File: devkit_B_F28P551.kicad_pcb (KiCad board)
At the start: 4 copper layers, 27 x 73.7 mm, 26 parts, among them J1 DEVKIT_C2000_ROW_A, J2 DEVKIT_C2000_ROW_B, J4 RESET, U1 TMS320F28P551SG5PM, U2 MCP1700-3302E/TT, U3 MCP1700-3302E/TT

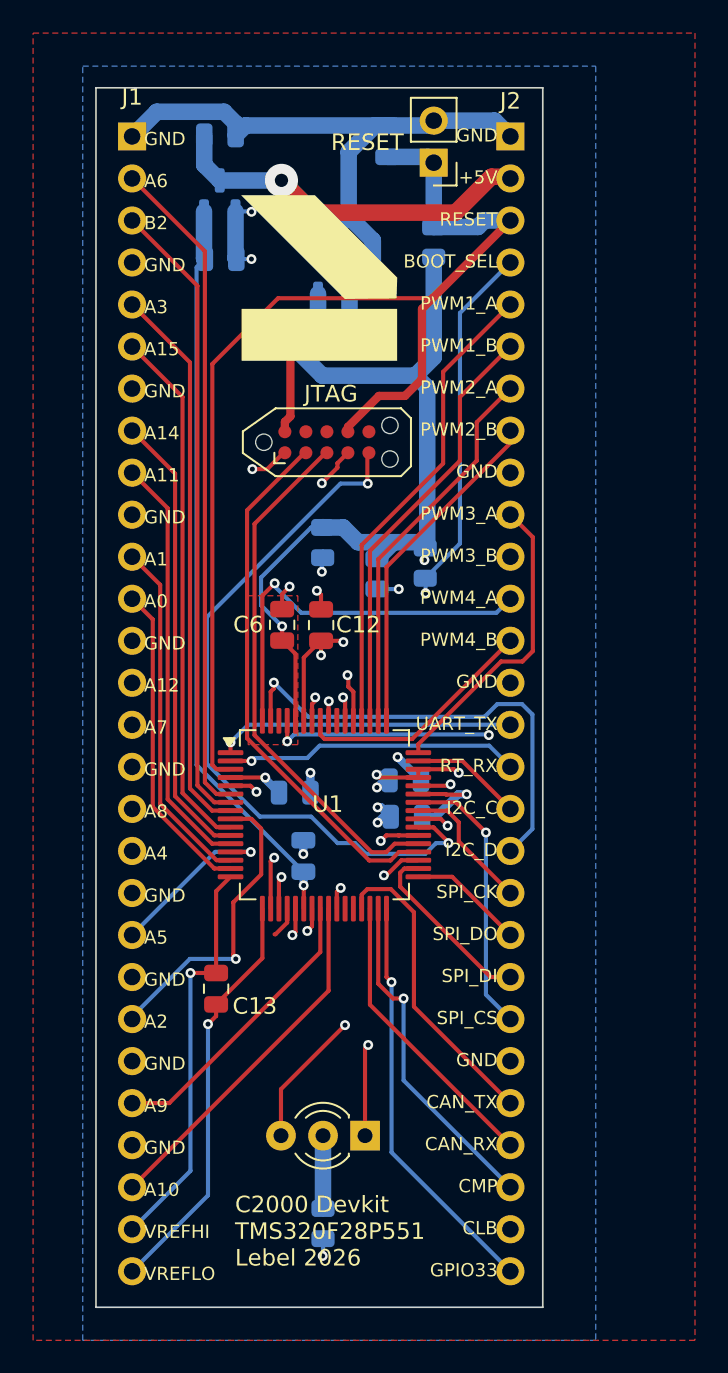
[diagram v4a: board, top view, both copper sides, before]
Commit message: devkit_B_F28P551 : rangee A reroutee pour le CLB (Stage1_EN/Stage2_EN/HV_EN/Discharge), documentation rattrapee
Carte figee, production-ready, modifiee malgre la regle habituelle (decision
explicite de l'utilisateur) : miroir de la decision #20 du depot
KICAD-C2000-powershield cote devkit.

- Rangee A reroutee : Stage1_EN (A23, broche 62/GPIO9), Stage2_EN (A24,
  broche 27/GPIO20), HV_EN (A25, broche 28/GPIO21), Discharge (A26, broche
  55/GPIO41) - six masses pour vingt-deux signaux au lieu de dix pour
  dix-huit.
- Rangee B : nRESET -> ~{RESET} (B3), GPIO_1 -> ~{FAULT_MCU} (B28), logique
  negative, meme net.
- devkit_A_F280037 non modifie (CLB absent du F280037) : le connecteur
  n'est plus identique entre les deux devkits, divergence documentee a la
  decision #13.
- doc/decisions.md : nouvelle decision #13.
- doc/spec-devkit.md, doc/brochage-devkit.csv : rangee A de devkit_B
  consignee comme bloc divergent, devkit_A_F280037 garde la rangee
  d'origine comme reference.

Verification avant commit : kicad-cli pcb drc sur devkit_B_F28P551.kicad_pcb
(0 violation, 0 non connecte) ; kicad-cli sch erc (35 violations, 10
erreurs/25 avertissements, toutes de type deja rencontre ailleurs dans
l'atelier - endpoint_off_grid, pin_not_connected -, aucune nouvelle
categorie).

Co-Authored-By: Claude Sonnet 5 <noreply@anthropic.com>
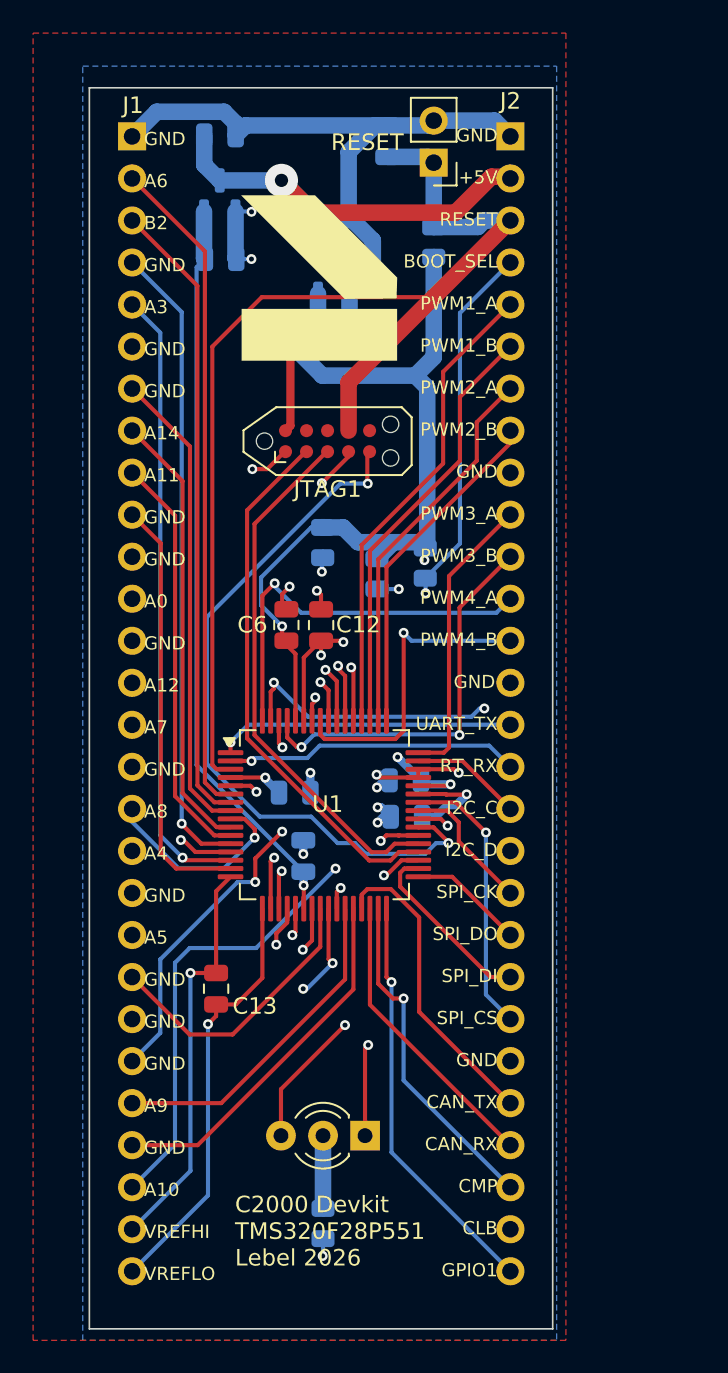
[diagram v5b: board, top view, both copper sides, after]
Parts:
- removed JTAG: Tag-Connect-2050_10, Connector:Tag-Connect_TC2050-IDC-NL_2x05_P1.27mm_Vertical
- added JTAG1: Tag-Connect-2050_10, Connector:Tag-Connect_TC2050-IDC-NL_2x05_P1.27mm_Vertical, F.Cu at (137.8, 65.7)
- moved C6 0.26 mm to (135.3, 76.8)
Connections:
- net GPIO_1 renamed ~{FAULT_MCU}
- net ~{nRESET} renamed ~{RESET}
- J1 pad 10: GND -> ADC_8
- J1 pad 11: Iout -> GND
- J1 pad 12: ADC_8 -> ADC_9
- J1 pad 13: GND -> ADC_10
- J1 pad 14: ADC_9 -> ADC_11
- J1 pad 15: ADC_10 -> ADC_12
- J1 pad 17: ADC_11 -> I_SHUNT1_CMP
- J1 pad 18: ADC_12 -> I_SHUNT1_MES
- J1 pad 20: I_SHUNT1_MES -> I_SHUNT2_CMP
- J1 pad 21: GND -> I_SHUNT2_MES
- J1 pad 22: I_SHUNT1_CMP -> GND
- J1 pad 23: GND -> Stage1_EN
- J1 pad 24: I_SHUNT2_MES -> Stage2_EN
- J1 pad 25: GND -> HV_EN
- J1 pad 26: I_SHUNT2_CMP -> Discharge
- J1 pad 4: GND -> Iin
- J1 pad 5: V1 -> Iout
- J1 pad 6: Temp1 -> GND
- J1 pad 7: GND -> V1
- J1 pad 8: Temp2 -> Temp1
- J1 pad 9: Iin -> Temp2
- U1 pad 27: TP_PIN27 -> Stage2_EN
- U1 pad 28: TP_PIN28 -> HV_EN
- U1 pad 55: TP_PIN55 -> Discharge
- U1 pad 62: TP_PIN62 -> Stage1_EN
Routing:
- net Discharge: track 0.00 -> 42.4 mm, vias 0 -> 2
- net Stage1_EN: track 0.00 -> 25.3 mm, vias 0 -> 3
- net HV_EN: track 0.00 -> 22.2 mm
- net Stage2_EN: track 0.00 -> 20.2 mm
- net Iout: track 21.3 -> 37.7 mm, vias 0 -> 1
- net Iin: track 25.5 -> 38.6 mm, vias 0 -> 1
- net ADC_11: track 13.6 -> 21.9 mm, vias 0 -> 1
- net ADC_12: track 14.9 -> 22.1 mm
- net ADC_8: track 19.3 -> 25.8 mm
- net I_SHUNT1_CMP: track 18.6 -> 12.3 mm
- net ADC_9: track 17.5 -> 23.3 mm
- net V1: track 33.7 -> 28.6 mm
- net Temp1: track 32.0 -> 26.9 mm
- net ADC_10: track 16.0 -> 20.8 mm
- net LED_R: track 30.0 -> 34.3 mm
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- removed copper zone on F.Cu, net VDDIO
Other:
- board size 27 x 73.7 mm -> 28 x 75 mm
- board text added: "GPIO1"
- board text removed: "A1"
- board text removed: "A15"
- board text removed: "A2"
- board text removed: "GPIO33"

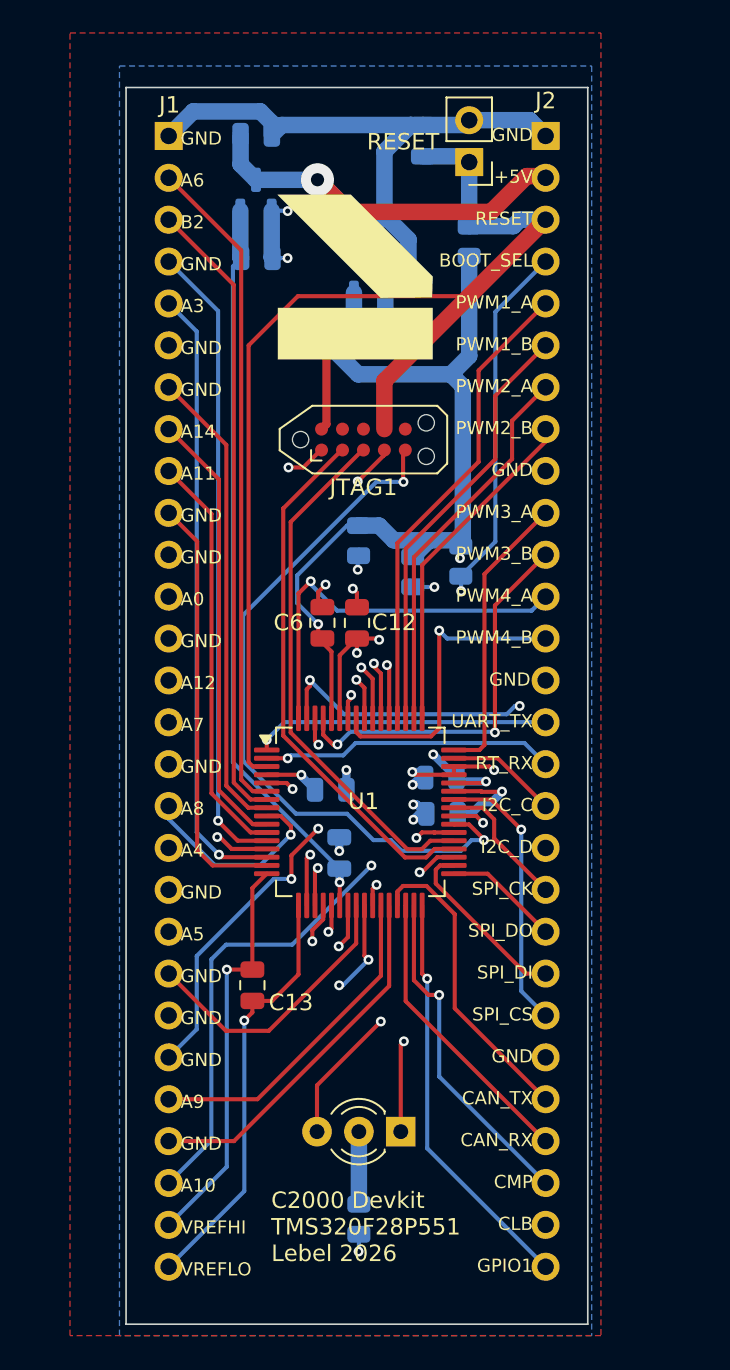
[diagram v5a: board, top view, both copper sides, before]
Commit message: Ajoute le connecteur RKB2SJM250SMTR_LFS et partage TO252
- Connecteur RKB2SJM250SMTR_LFS (lib + modele 3D) integre au connecteur
  devkit, modification de brochage associee (modificatio_brochage_devkit)
  -- travail deja en place localement, jamais commite.
- fp-lib-table : empreinte TO252 partagee enregistree
  (lib_fp_commun/TO252.pretty, voir KICAD.md), pas encore utilisee par
  un composant de ce depot.

Co-Authored-By: Claude Sonnet 5 <noreply@anthropic.com>
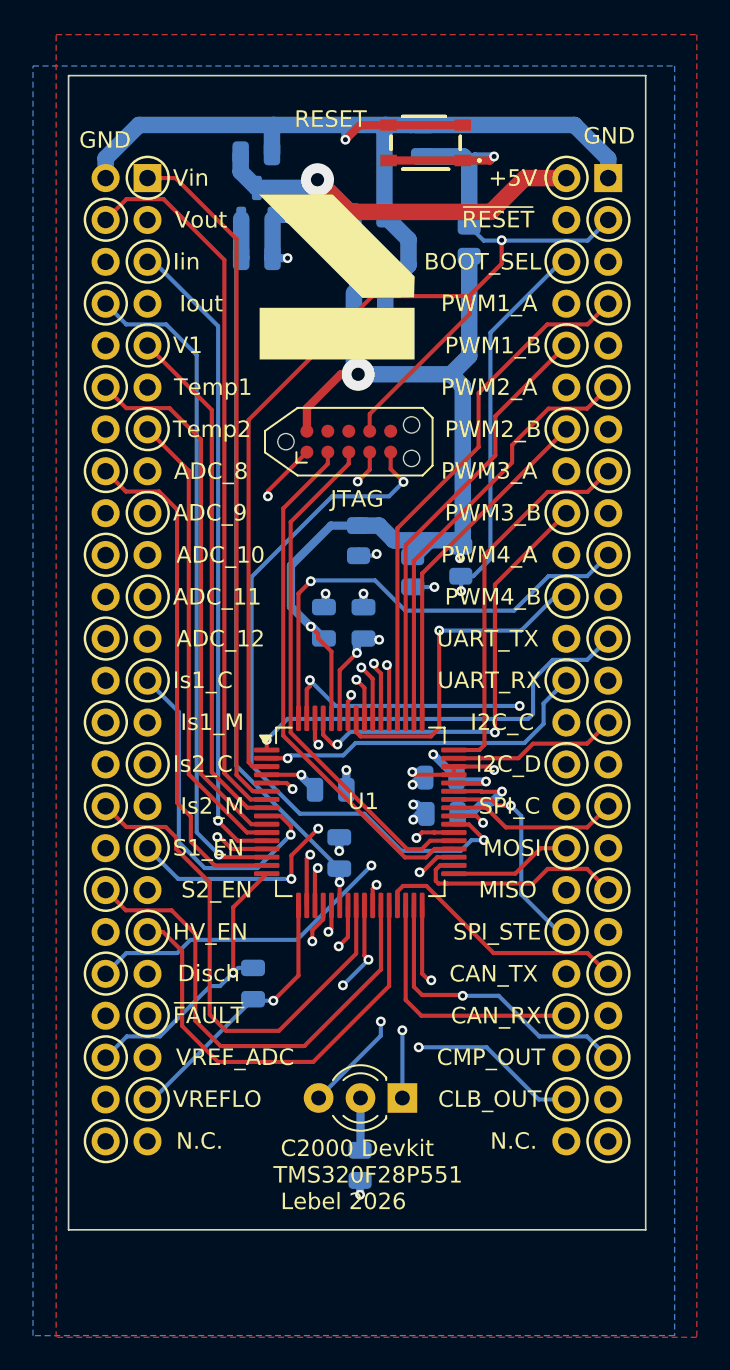
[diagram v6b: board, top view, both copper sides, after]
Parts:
- removed J4: RESET, Connector_PinHeader_2.54mm:PinHeader_1x02_P2.54mm_Vertical
- added S1: RKB2SJM250SMTR_LFS, lib:RKB2SJM250SMTRLFS, F.Cu at (141.6, 47.7)
- C12, C13, C6: moved to B.Cu
- J1: value DEVKIT_C2000_ROW_A -> DEVKIT_C2000_A; footprint Connector_PinHeader_2.54mm:PinHeader_1x28_P2.54mm_Vertical -> Connector_PinHeader_2.54mm:PinHeader_2x24_P2.54mm_Vertical
- J2: value DEVKIT_C2000_ROW_B -> DEVKIT_C2000_B; footprint Connector_PinHeader_2.54mm:PinHeader_1x28_P2.54mm_Vertical -> Connector_PinHeader_2.54mm:PinHeader_2x24_P2.54mm_Vertical
- moved J2 4.58 mm to (152.6, 49.8)
- moved R5 3.27 mm to (137.6, 109.7)
- moved J1 2.86 mm to (124.7, 49.8)
- moved D1 2.04 mm to (140.2, 105.6)
- moved C3 1.12 mm to (131.3, 48.3)
- moved G*** 1.10 mm to (136.5, 55.8)
- moved JTAG1 0.90 mm to (136.9, 65.8)
- moved U3 0.50 mm to (131.3, 51.3)
- moved C12 0.40 mm to (137.8, 76.8)
- moved C13 0.11 mm to (131.1, 98.7)
- moved C6 0.09 mm to (135.4, 76.8)
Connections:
- J1 pad 1: GND -> Vin
- J1 pad 10: ADC_8 -> GND
- J1 pad 12: ADC_9 -> Temp1
- J1 pad 13: ADC_10 -> Temp2
- J1 pad 14: ADC_11 -> GND
- J1 pad 15: ADC_12 -> GND
- J1 pad 16: GND -> ADC_8
- J1 pad 17: I_SHUNT1_CMP -> ADC_9
- J1 pad 18: I_SHUNT1_MES -> GND
- J1 pad 2: Vin -> GND
- J1 pad 20: I_SHUNT2_CMP -> ADC_10
- J1 pad 21: I_SHUNT2_MES -> ADC_11
- J1 pad 23: Stage1_EN -> GND
- J1 pad 24: Stage2_EN -> ADC_12
- J1 pad 25: HV_EN -> I_SHUNT1_CMP
- J1 pad 26: Discharge -> GND
- J1 pad 27: VREF_ADC -> GND
- J1 pad 28: VREFLO_SENSE -> I_SHUNT1_MES
- J1 pad 3: Vout -> GND
- J1 pad 4: Iin -> Vout
- J1 pad 5: Iout -> Iin
- J1 pad 7: V1 -> GND
- J1 pad 8: Temp1 -> Iout
- J1 pad 9: Temp2 -> V1
- J2 pad 10: PWM3_A -> PWM1_B
- J2 pad 11: PWM3_B -> PWM2_A
- J2 pad 12: PWM4_A -> GND
- J2 pad 13: PWM4_B -> GND
- J2 pad 14: GND -> PWM2_B
- J2 pad 15: UART_TX -> PWM3_A
- J2 pad 16: UART_RX -> GND
- J2 pad 17: I2C_SCL -> GND
- J2 pad 18: I2C_SDA -> PWM3_B
- J2 pad 19: SPI_CLK -> PWM4_A
- J2 pad 20: SPI_SIMO -> GND
- J2 pad 21: SPI_SOMI -> GND
- J2 pad 22: SPI_STE -> PWM4_B
- J2 pad 23: GND -> UART_TX
- J2 pad 24: CAN_TX -> GND
- J2 pad 25: CAN_RX -> GND
- J2 pad 26: CMP_OUT -> UART_RX
- J2 pad 27: CLB_OUT -> I2C_SCL
- J2 pad 28: ~{FAULT_MCU} -> GND
- J2 pad 4: BOOT_SEL -> GND
- J2 pad 5: PWM1_A -> GND
- J2 pad 6: PWM1_B -> BOOT_SEL
- J2 pad 7: PWM2_A -> PWM1_A
- J2 pad 8: PWM2_B -> GND
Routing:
- net GND: track 68.9 -> 87.2 mm, vias 17 -> 18
- net I_SHUNT2_MES: track 17.3 -> 30.8 mm
- net ADC_12: track 22.1 -> 31.9 mm
- net VREFLO_SENSE: track 25.9 -> 16.6 mm
- net Stage2_EN: track 20.2 -> 29.5 mm
- net I_SHUNT1_CMP: track 12.3 -> 21.1 mm
- net I_SHUNT2_CMP: track 17.5 -> 26.1 mm
- net ADC_10: track 20.8 -> 29.3 mm
- net ~{RESET}: track 69.5 -> 77.7 mm, vias 0 -> 2
- net I_SHUNT1_MES: track 6.52 -> 14.4 mm
- net Discharge: track 42.4 -> 34.5 mm
- net UART_TX: track 18.0 -> 25.1 mm
- net VREF_ADC: track 24.7 -> 18.0 mm
- net ADC_11: track 21.9 -> 28.3 mm
- net Temp1: track 26.9 -> 32.6 mm
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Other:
- board size 28 x 75 mm -> 35 x 70 mm
- board text added: "ADC_10"
- board text added: "ADC_11"
- board text added: "ADC_12"
- board text added: "ADC_8"
- board text added: "ADC_9"
- board text added: "CLB_OUT"
- board text added: "CMP_OUT"
- board text added: "Disch"
- board text added: "HV_EN"
- board text added: "Iin"
- board text added: "Iout"
- board text added: "Is1_C"
- board text added: "Is1_M"
- board text added: "Is2_C"
- board text added: "Is2_M"
- board text added: "JTAG"
- board text added: "MISO"
- board text added: "MOSI"
- board text added: "N.C."
- board text added: "S1_EN"
- board text added: "S2_EN"
- board text added: "SPI_C"
- board text added: "SPI_STE"
- board text added: "Temp1"
- board text added: "Temp2"
- board text added: "UART_RX"
- board text added: "V1"
- board text added: "VREF_ADC"
- board text added: "Vin"
- board text added: "Vout"
- board text added: "~{FAULT}"
- board text added: "~{RESET}"
- board text removed: "A0"
- board text removed: "A10"
- board text removed: "A11"
- board text removed: "A12"
- board text removed: "A14"
- board text removed: "A3"
- board text removed: "A4"
- board text removed: "A5"
- board text removed: "A6"
- board text removed: "A7"
- board text removed: "A8"
- board text removed: "A9"
- board text removed: "B2"
- board text removed: "CLB"
- board text removed: "CMP"
- board text removed: "GPIO1"
- board text removed: "RT_RX"
- board text removed: "SPI_CK"
- board text removed: "SPI_CS"
- board text removed: "SPI_DI"
- board text removed: "SPI_DO"
- board text removed: "VREFHI"
